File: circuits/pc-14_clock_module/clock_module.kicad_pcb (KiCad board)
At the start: 2 copper layers, 99.1 x 99.1 mm, 8 parts

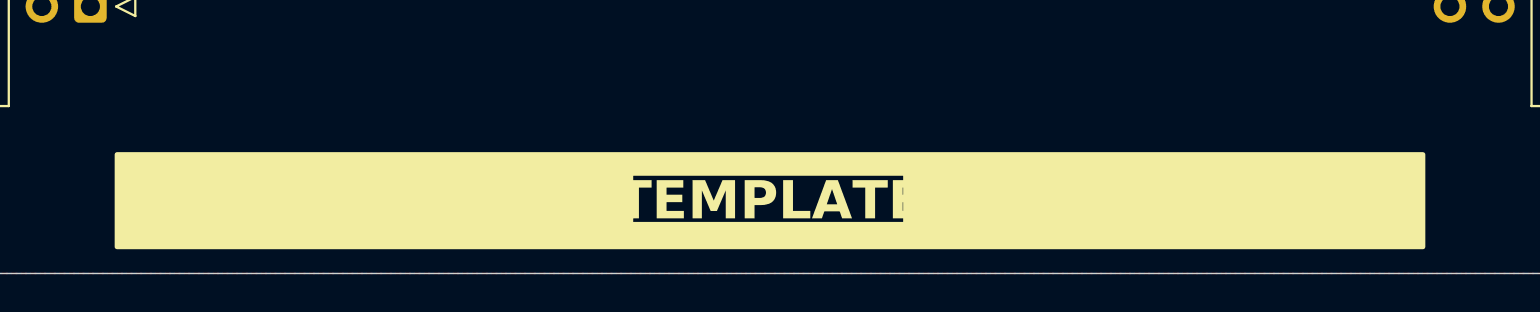
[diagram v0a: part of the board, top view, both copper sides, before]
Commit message: pc-14: continue clock module: full functionality and power-on reset logic.
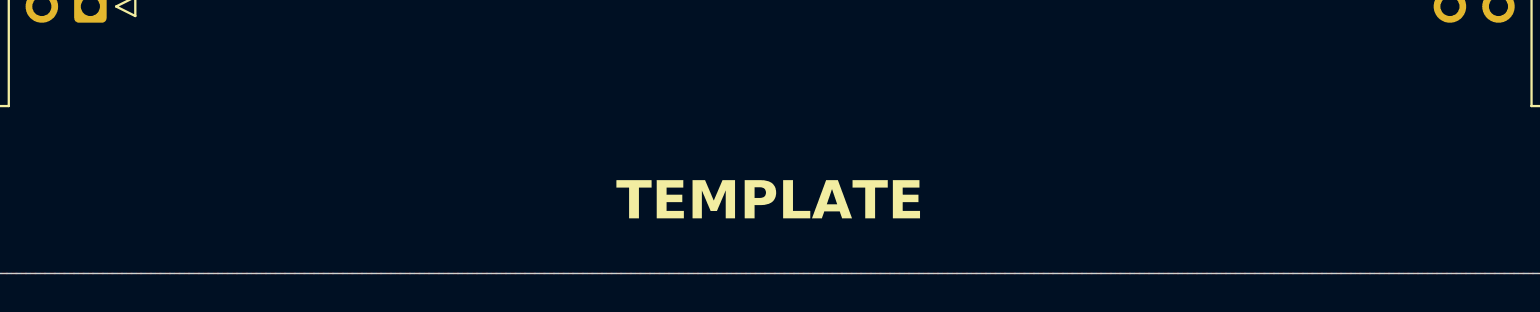
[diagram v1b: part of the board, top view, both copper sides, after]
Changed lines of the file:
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@@
 		(min_thickness 0.25)
 		(filled_areas_thickness no)
-		(fill yes
+		(fill
 			(thermal_gap 0.5)
 			(thermal_bridge_width 0.5)
@@
 		(min_thickness 0.25)
 		(filled_areas_thickness no)
-		(fill yes
+		(fill
 			(thermal_gap 0.5)
 			(thermal_bridge_width 0.5)
@@
 		(min_thickness 0.25)
 		(filled_areas_thickness no)
-		(fill yes
+		(fill
 			(thermal_gap 0.5)
 			(thermal_bridge_width 0.5)
